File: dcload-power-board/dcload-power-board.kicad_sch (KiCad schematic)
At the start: 32 parts, among them J100 Conn_01x08_Male, J101 Conn_01x08_Male, J103 Conn_01x02_Male, U100 NCP718BSN500, U101 TLV431C, U102 TMUX1101, U103 NCS20231

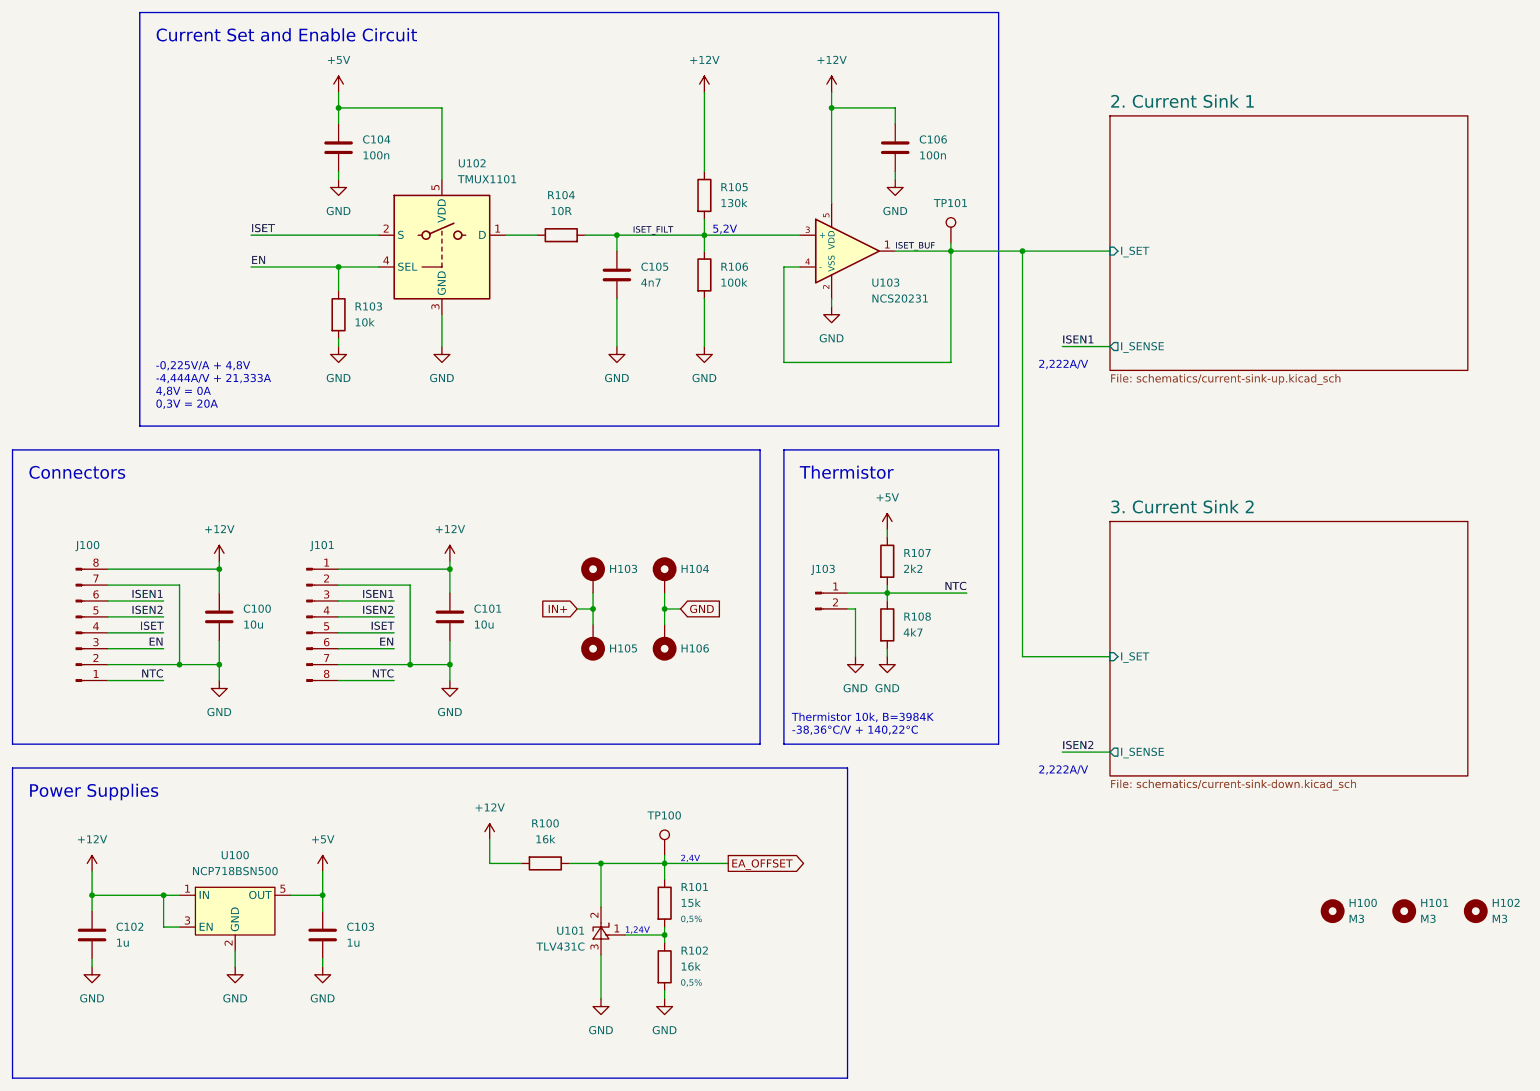
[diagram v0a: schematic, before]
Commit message: add: interface panel board
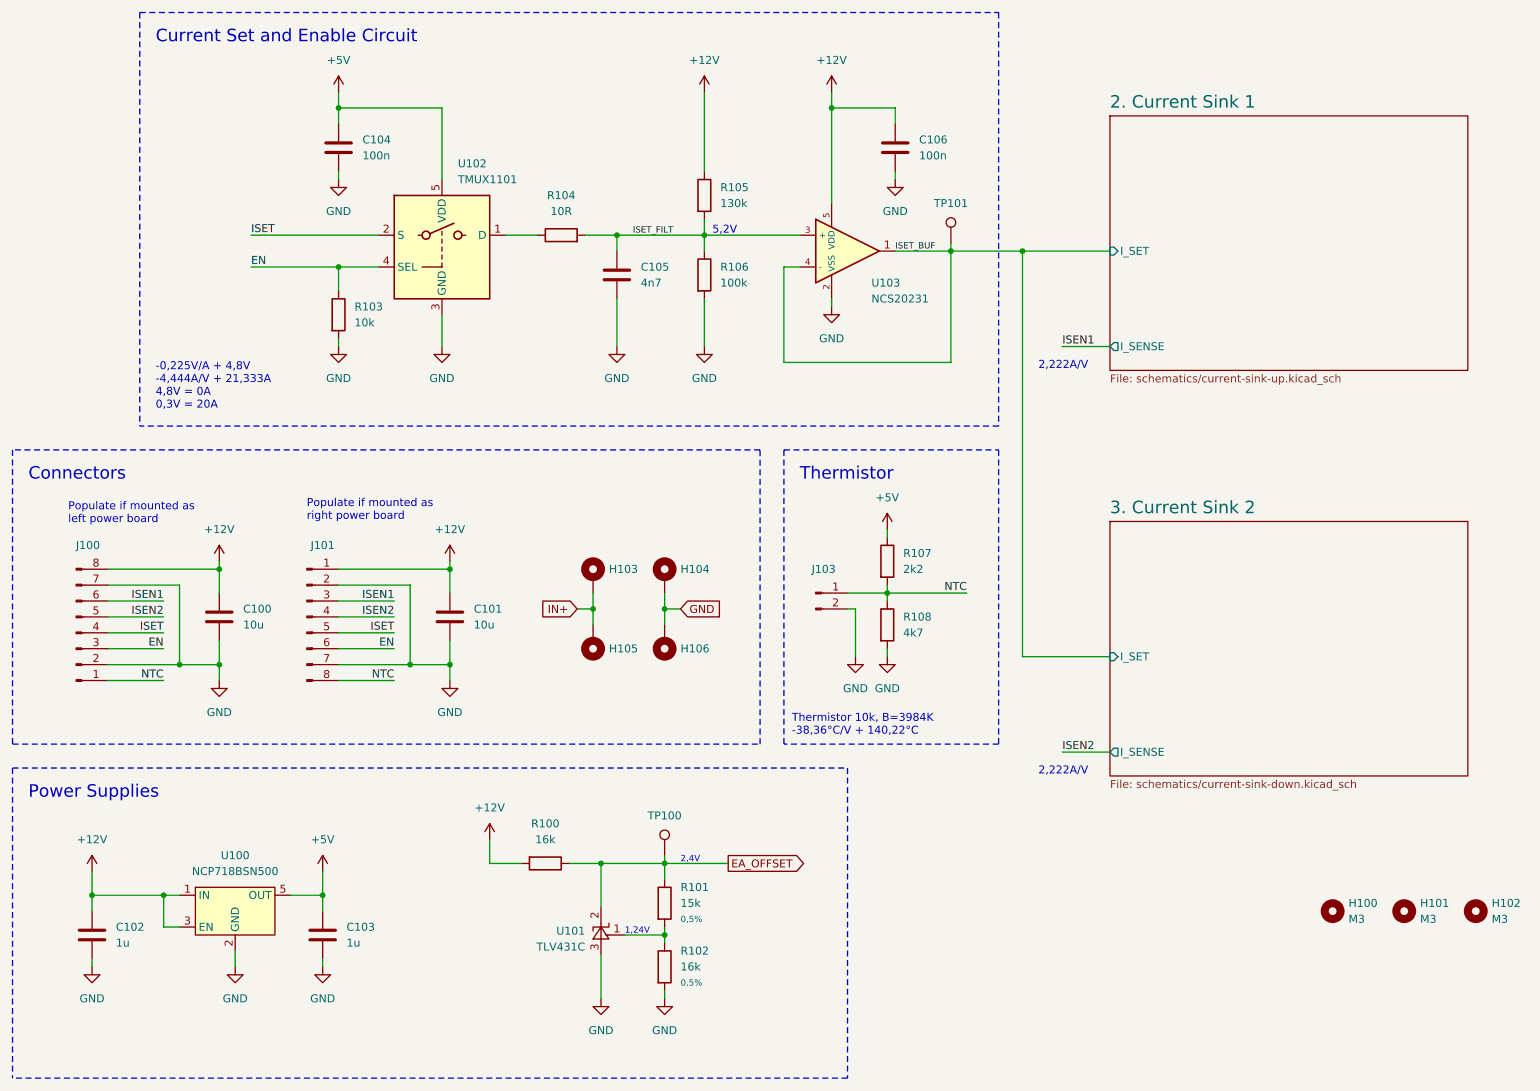
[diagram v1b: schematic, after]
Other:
- note added: "Populate if mounted as left power board"
- note added: "Populate if mounted as right power board"
